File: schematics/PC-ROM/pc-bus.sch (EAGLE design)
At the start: 20 parts

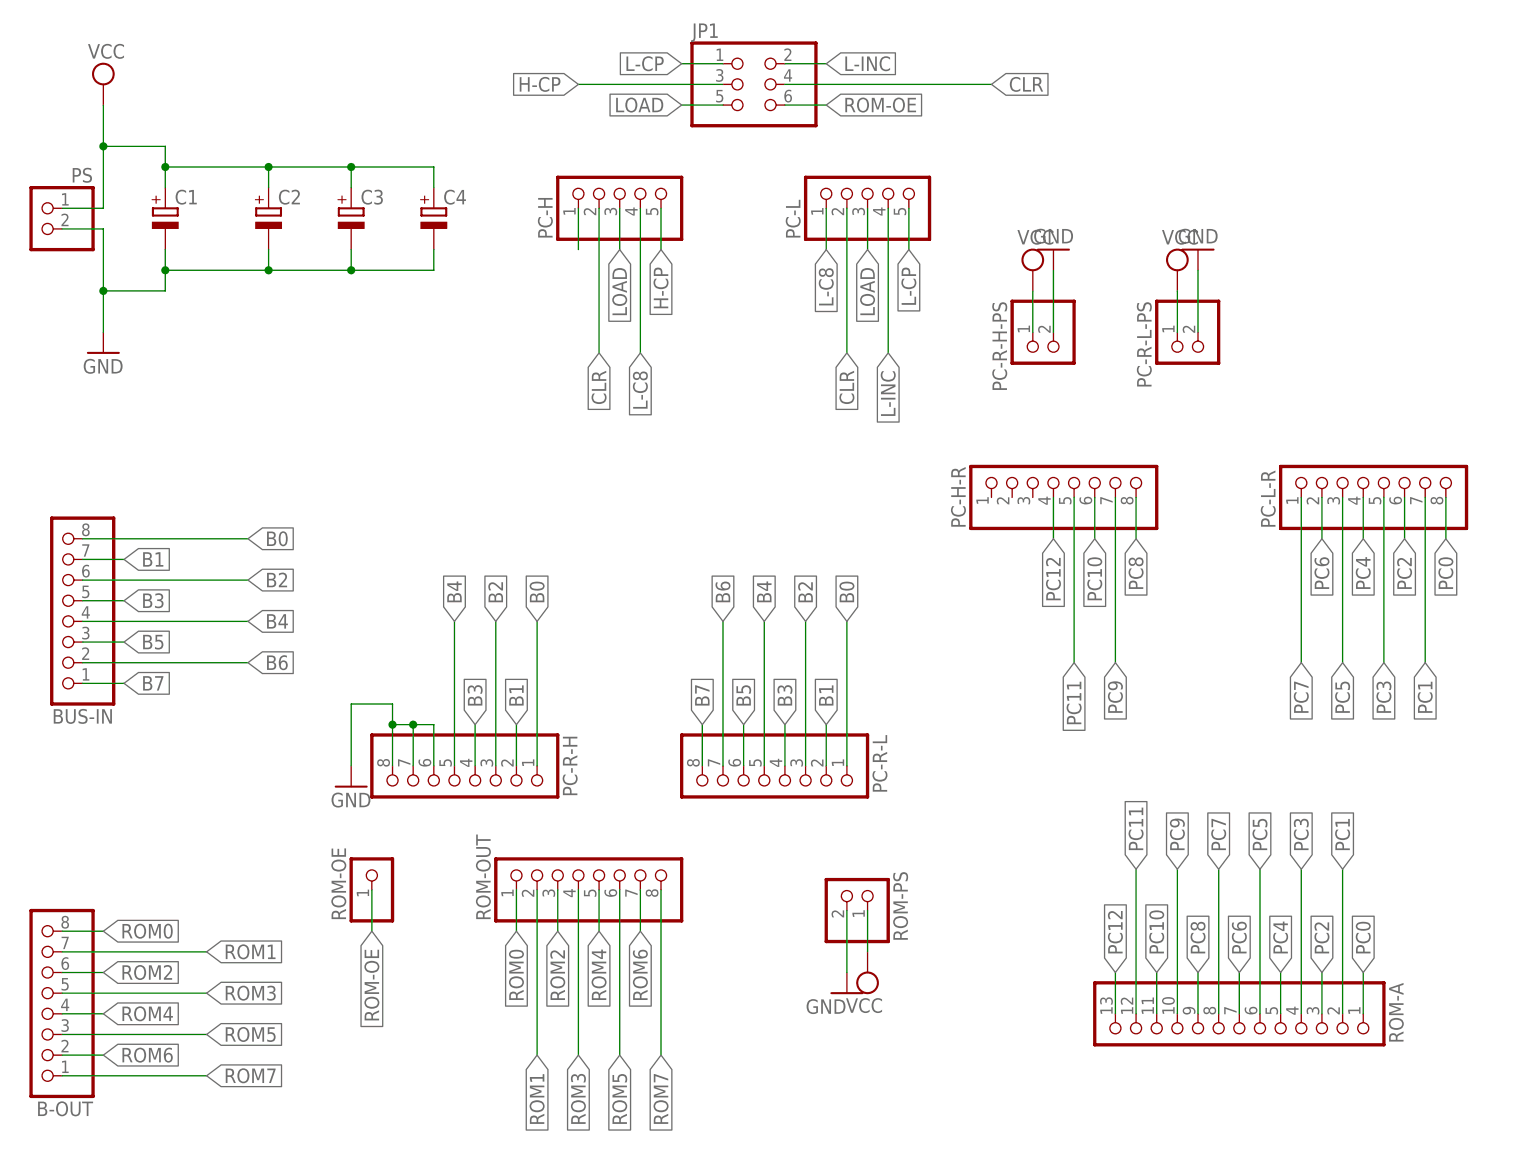
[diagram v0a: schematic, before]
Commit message: Added resistors to rom address.
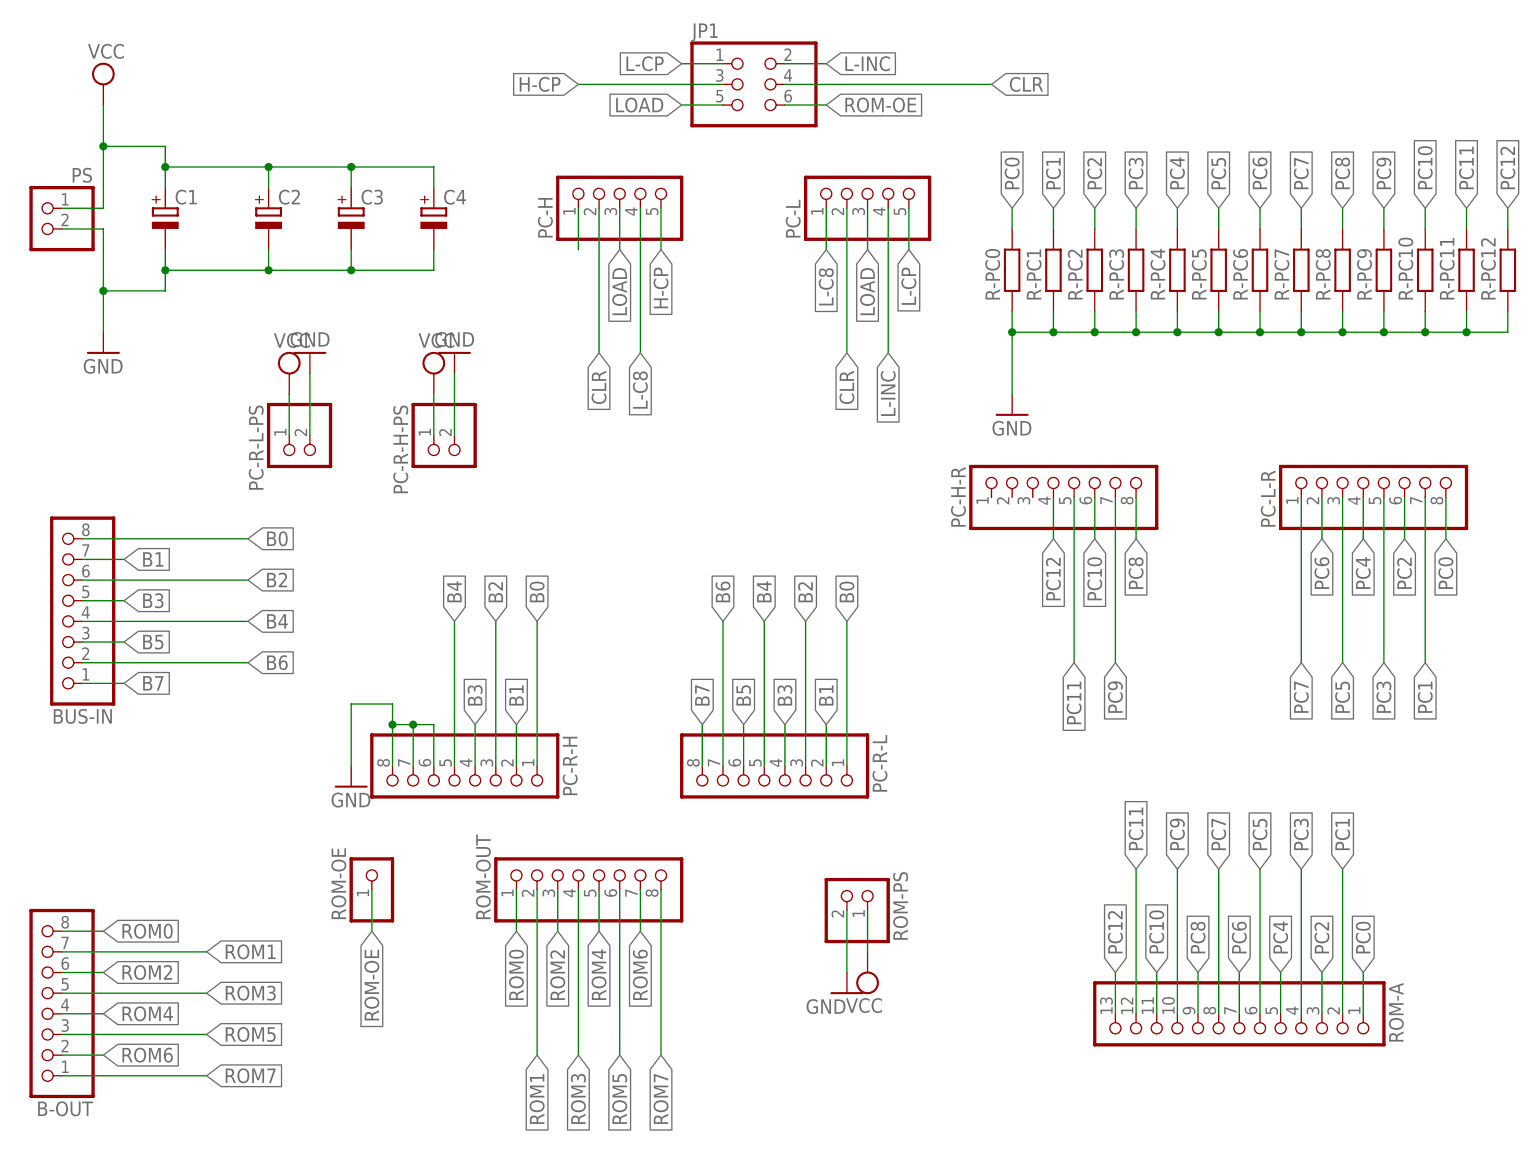
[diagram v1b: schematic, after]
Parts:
- added R-PC0, R-PC1, R-PC10, R-PC11, R-PC12, R-PC2, R-PC3, R-PC4, R-PC5, R-PC6, R-PC7, R-PC8, R-PC9: (no value), rcl:R-EU_0204/7
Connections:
- net GND: now also R-PC0.1, R-PC1.1, R-PC10.1, R-PC11.1, R-PC12.1, R-PC2.1, R-PC3.1, R-PC4.1, R-PC5.1, R-PC6.1, R-PC7.1, R-PC8.1, R-PC9.1
- net PC0: now also R-PC0.2
- net PC1: now also R-PC1.2
- net PC10: now also R-PC10.2
- net PC11: now also R-PC11.2
- net PC12: now also R-PC12.2
- net PC2: now also R-PC2.2
- net PC3: now also R-PC3.2
- net PC4: now also R-PC4.2
- net PC5: now also R-PC5.2
- net PC6: now also R-PC6.2
- net PC7: now also R-PC7.2
- net PC8: now also R-PC8.2
- net PC9: now also R-PC9.2
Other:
- moved on the sheet: PC-R-H-PS, PC-R-L-PS
